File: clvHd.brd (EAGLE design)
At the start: 21 x 35 mm, 41 parts, among them IC1 LMV324M, X1 009176002, X2 009176002, X3 SSW-101-02-G-S, X4 009176002, X5 SSW-101-02-G-S, X6 009176002, X7 SSW-101-02-G-S

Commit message: update
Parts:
- removed A1, A2: 0R-JUMPC, jump-0r-smd:C0R-JMP
- removed ADC: MICROCHIP_MCP3427-E-UNMICROCHIP_MCP3427-E-UN_0_0, UN:MICROCHIP_MCP3427-E-UN_0
- removed C1, C3, C4, C5, C6, C7, C8, C9: 0.1nF, rcl:C0201
- removed C2: 1nF, rcl:C0201
- removed D3: HSMS-285C, avago:SOT323
- removed IC1: LMV324M, linear:SO14
- removed L: (no value), led:CHIP-LED0603
- removed P_AMP: INA326EA/250, INA326EA_250:SOP65P490X110-8N
- removed R1, R10, R11, R12, R13, R14, R16, R17, R2, R3, R4, R5, R6, R7, R8, R9: 100k, rcl:R0201
- removed R15: (no value), rcl:R0201
- removed TLE: TLE2426CD, tle2426:SO-8
- removed X1, X2, X4, X6: 009176002, con-avxPerso:009176002
- removed X3, X5, X7: SSW-101-02-G-S, con-samtec:SSW-101-02-G-S
- added LED1, LED2, LED3: (no value), led:CHIP-LED0603
- added PAD1, PAD10, PAD11, PAD12, PAD2, PAD3, PAD4, PAD5, PAD6, PAD7, PAD8, PAD9: WIREPADSMD1,27-254, wirepad:SMD1,27-2,54
- added U1: ADS1298CZXGR, ADS1298ZXGR:ZXG64
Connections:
- removed net GNDA: ADC.2, ADC.5, C2.1, IC1.12, IC1.3, IC1.5, R12.1, R2.1, R5.2, TLE.1, X7.1
- removed net INM: P_AMP.2, X3.1
- removed net INP: P_AMP.3, X5.1
- removed net N$1: P_AMP.1, R1.1
- removed net N$10: IC1.6, R6.2, R7.1, R8.1
- removed net N$11: D3.2, R14.2, R8.2
- removed net N$12: IC1.9, R10.1, R9.2
- removed net N$13: D3.3, IC1.7
- removed net N$14: D3.1, R7.2, R9.1
- removed net N$15: IC1.8, R10.2, R11.1
- removed net N$16: ADC.1, C5.2, IC1.14, R4.2
- removed net N$17: ADC.7, R16.2, X2.1, X6.1
- removed net N$18: IC1.10, R12.2, R14.1
- removed net N$2: P_AMP.8, R1.2
- removed net N$23: ADC.4, C4.1, IC1.1, R3.2, R6.1
- removed net N$4: C2.2, P_AMP.5, R2.2
- removed net N$54: L.A, R15.2
- removed net N$55: C7.1, TLE.8
- removed net N$56: ADC.8, R17.2, X2.2, X6.2
- removed net N$57: A1.2, ADC.9
- removed net N$58: A2.2, ADC.10
- removed net N$6: C3.1, IC1.2, R3.1
- removed net N$7: C3.2, C4.2, R13.2, R5.1
- removed net N$8: C5.1, IC1.13, R11.2, R4.1
- removed net N$9: P_AMP.6, R13.1
- removed net V+: A1.3, A2.3, ADC.6, C1.1, C6.1, C8.2, C9.2, IC1.4, P_AMP.7, R15.1, R16.1, R17.1, TLE.3, X1.2, X4.2
- removed net V-: A1.1, A2.1, ADC.3, C1.2, C6.2, C7.2, C8.1, C9.1, IC1.11, L.C, P_AMP.4, TLE.2, X1.1, X4.1
- new net IN1: U1.H1
- new net IN2: U1.G1
- new net REF: U1.G2, U1.H2
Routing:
- net V-: track 99.1 -> 0.00 mm, vias 7 -> 0
- net V+: track 84.2 -> 0.00 mm
- net N$17: track 44.6 -> 0.00 mm, vias 3 -> 0
- net GNDA: track 36.9 -> 0.00 mm, vias 5 -> 0
- net N$56: track 34.4 -> 0.00 mm, vias 3 -> 0
- net INP: track 34.3 -> 0.00 mm, vias 1 -> 0
- net N$9: track 25.4 -> 0.00 mm, vias 0 -> 1
- net N$23: track 23.5 -> 0.00 mm, vias 2 -> 0
- net N$8: track 17.8 -> 0.00 mm, vias 2 -> 1
- net N$10: track 16.8 -> 0.00 mm, vias 2 -> 1
- net N$6: track 13.3 -> 0.00 mm, vias 0 -> 1
- net N$12: track 12.1 -> 0.00 mm, vias 0 -> 1
- net N$13: track 10.4 -> 0.00 mm, vias 0 -> 1
- net N$16: track 8.56 -> 0.00 mm, vias 0 -> 1
- net N$7: track 8.02 -> 0.00 mm, vias 0 -> 1
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- added copper zone on layer 16, net IN1
- added copper zone on layer 16, net IN3
- added copper zone on layer 16, net IN4
- added copper zone on layer 16, net IN5
- added copper zone on layer 16, net IN6
- added copper zone on layer 16, net IN7
- added copper zone on layer 16, net IN8
- added copper zone on layer 16, net IN9
- added copper zone on layer 16, net REF
- removed copper zone on layer 16, net GNDA
- removed copper zone on layer 16, net INM
- removed copper zone on layer 16, net INP
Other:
- board size 21 x 35 mm -> 31 x 24 mm
- board text removed: "+"
- board text removed: "ClvHd"
- board text removed: "E+"
- board text removed: "E-"
- board text removed: "GND"
- board text removed: "SCL"
- board text removed: "SDA"
- board text removed: "V++"
- board text removed: "v7"

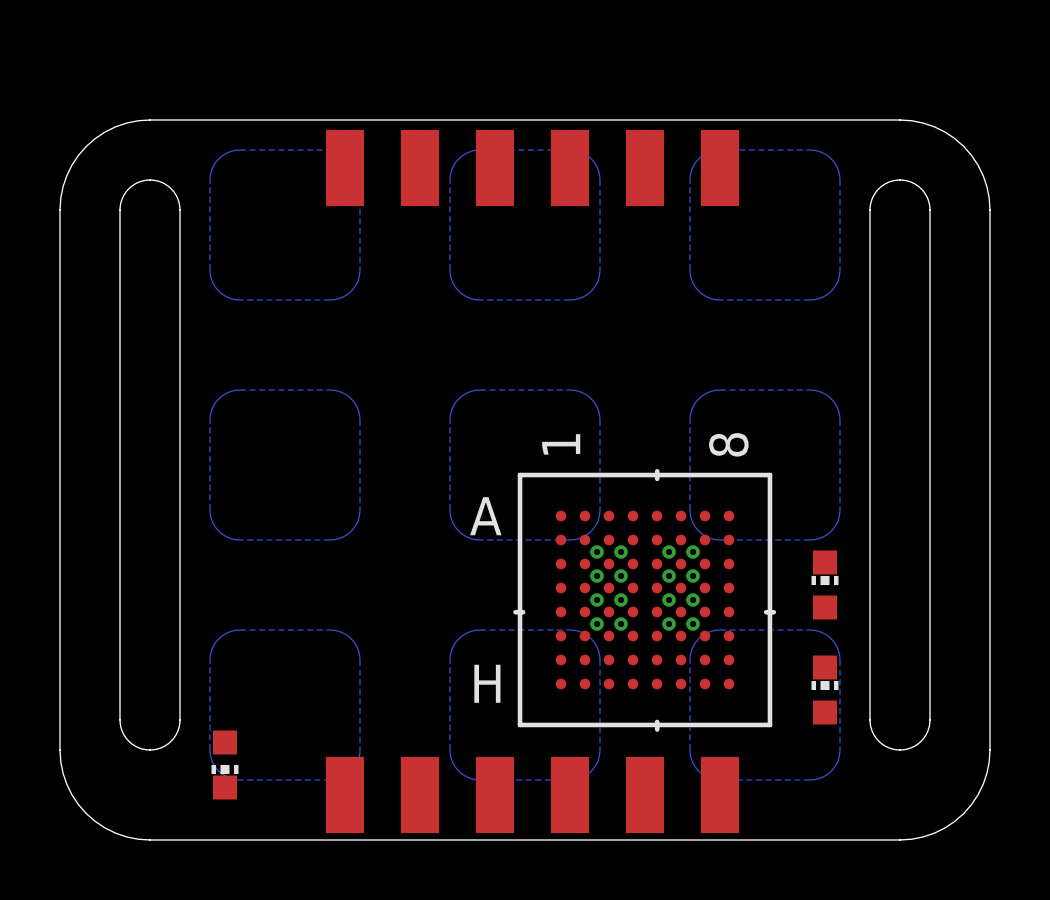
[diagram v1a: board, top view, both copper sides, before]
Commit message: jst sh conn
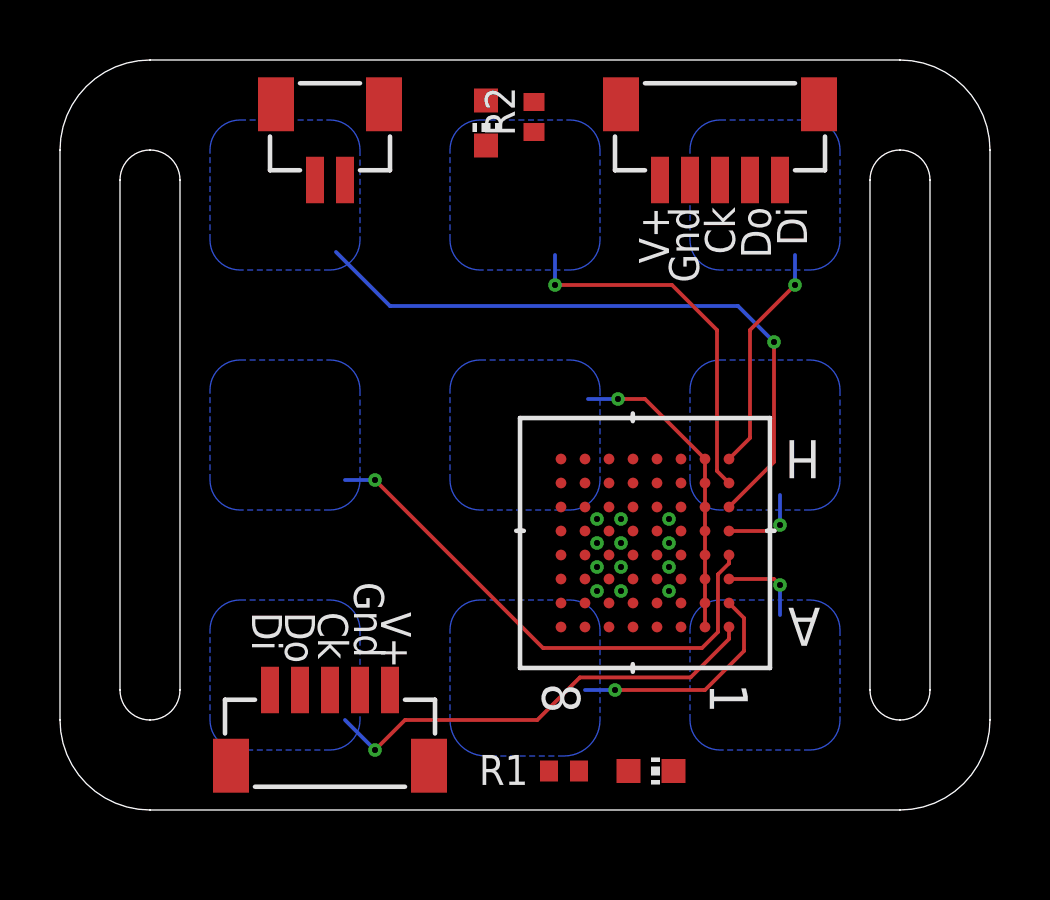
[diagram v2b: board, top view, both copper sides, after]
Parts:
- removed LED3: (no value), led:CHIP-LED0603
- removed PAD1, PAD10, PAD11, PAD12, PAD2, PAD3, PAD4, PAD5, PAD6, PAD7, PAD8, PAD9: WIREPADSMD1,27-254, wirepad:SMD1,27-2,54
- added R1, R2: (no value), rcl:R0402
- added X1: BM02B-SRSS-TB, con-JST SH:BM02B-SRSS-TB
- added X2, X3: BM05B-SRSS-TB, con-JST SH:BM05B-SRSS-TB
- moved LED2 22.0 mm to (14.2, 22.9), turned to 180 degrees
- moved LED1 14.2 mm to (19.7, 1.30), turned to 270 degrees
- moved U1 1.90 mm to (19.5, 8.90), turned to 180 degrees
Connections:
- new net CLK: X2.3, X3.3
- new net CS: U1.F7, X1.1
- new net DIN: X2.5, X3.5
- new net DOUT: X2.4, X3.4
- new net GND: R1.1, R2.1, X2.2, X3.2
- new net IN3: U1.C1
- new net IN4: U1.D1
- new net IN5: U1.E1
- new net IN6: U1.F1
- new net IN7: U1.G1
- new net IN8: U1.H1
- new net N$1: LED1.A, R1.2
- new net N$5: LED2.C, U1.F5
- new net N$6: LED2.A, R2.2
- new net V+: LED1.C, X2.1, X3.1
- net IN1: now also U1.A1; no longer U1.H1
- net IN2: now also U1.B1; no longer U1.G1
- net REF: now also U1.A2, U1.B2, U1.C2, U1.D2, U1.E2, U1.F2, X1.2
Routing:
- net IN6: track 0.00 -> 22.0 mm, vias 0 -> 1
- net IN4: track 0.00 -> 17.7 mm, vias 0 -> 1
- net IN1: track 0.00 -> 15.1 mm, vias 0 -> 1
- net IN7: track 0.00 -> 12.3 mm, vias 0 -> 1
- net REF: track 0.00 -> 10.3 mm, vias 0 -> 1
- net IN8: track 0.00 -> 7.71 mm, vias 0 -> 1
- net IN2: track 0.00 -> 7.65 mm, vias 0 -> 1
- net IN3: track 0.00 -> 2.78 mm, vias 0 -> 1
- net IN5: track 0.00 -> 2.78 mm, vias 0 -> 1
- added copper zone on layer 16, net IN2
- removed copper zone on layer 16, net IN9
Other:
- board size 31 x 24 mm -> 31 x 25 mm
- board text added: "Ck"
- board text added: "Di"
- board text added: "Do"
- board text added: "Gnd"
- board text added: "V+"

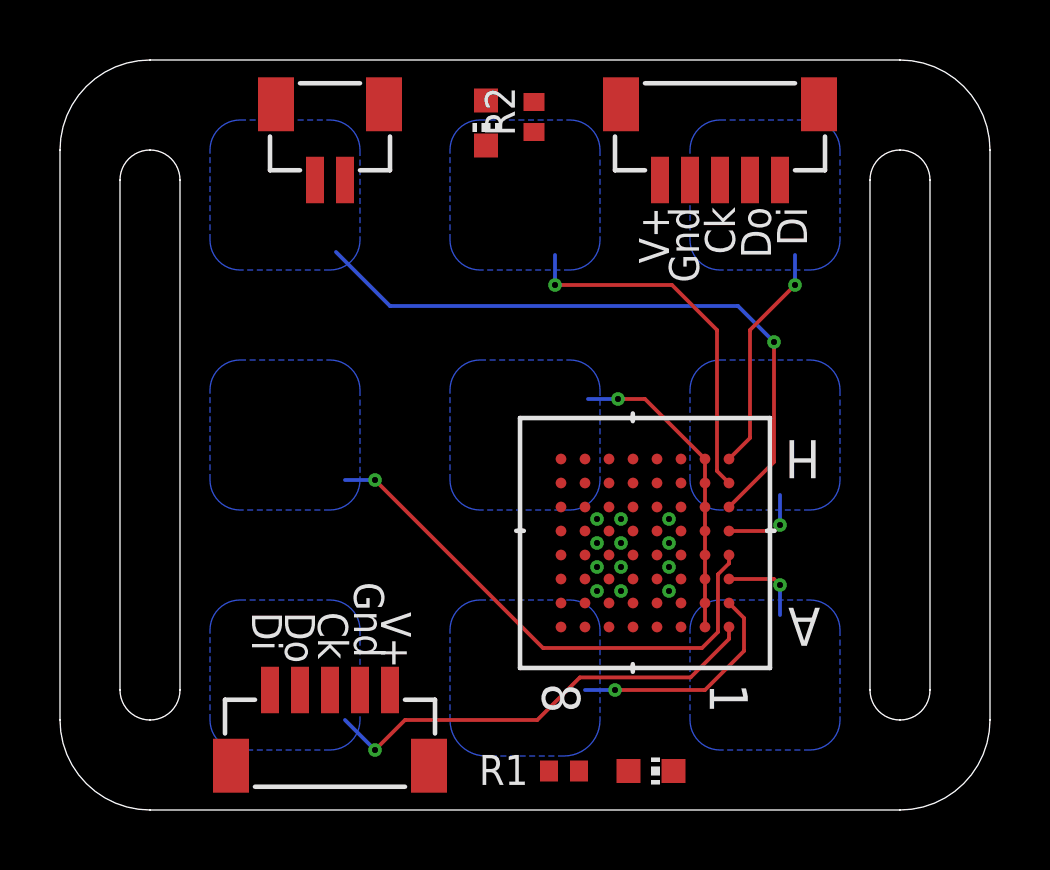
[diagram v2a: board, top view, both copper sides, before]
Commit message: dim changed to be panalized 3x4
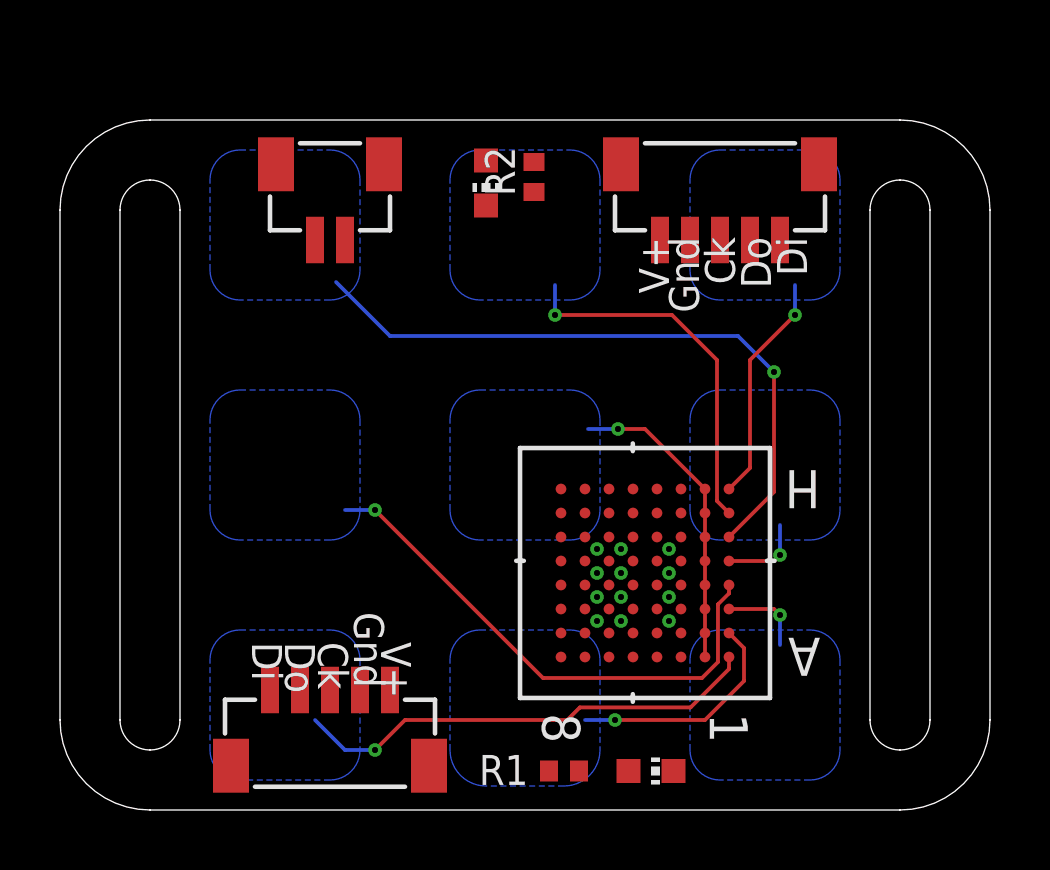
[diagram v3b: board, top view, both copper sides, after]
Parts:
- moved LED2 2.00 mm to (14.2, 20.9)
- moved R2 2.00 mm to (15.8, 21.1)
- moved X1 2.00 mm to (9.00, 19.0)
- moved X2 2.00 mm to (22.0, 19.0)
- moved U1 1.00 mm to (19.5, 7.90)
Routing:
- net IN1: track 15.1 -> 15.7 mm
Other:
- board size 31 x 25 mm -> 31 x 23 mm

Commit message: update
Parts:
- added C1, C10, C11, C12, C13, C14, C15, C16, C2, C3, C4, C5, C6, C7, C8, C9: 4.70nF, rcl:C0201
- added R10, R11, R12, R13, R14, R15, R16, R3, R4, R5, R6, R7, R8, R9: 4.99k, rcl:R0201
- R1, R2: value (none) -> 4.99k; device rcl:R0402 -> rcl:R0201
- U1: value ADS1298CZXGR -> ADS1299IPAG; device ADS1298ZXGR:ZXG64 -> ADS:PAG64_TEX
- X2, X3: value BM05B-SRSS-TB -> BM07B-SRSS-TB; device con-JST SH:BM05B-SRSS-TB -> con-JST SH:BM07B-SRSS-TB
- moved LED2 22.5 mm to (35.2, 12.9)
- moved R2 16.8 mm to (8.50, 6.00), turned to 0 degrees
- moved X2 16.3 mm to (9.50, 29.4)
- moved X1 13.4 mm to (17.5, 29.4)
- moved R1 12.2 mm to (5.50, 6.00)
- moved U1 9.01 mm to (16.8, 16.5), turned to 0 degrees
- moved LED1 4.24 mm to (15.7, 2.70), turned to 0 degrees
- moved X3 0.63 mm to (9.50, 3.61)
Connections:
- removed net CLK: X2.3, X3.3
- removed net IN1: U1.A1
- removed net IN2: U1.B1
- removed net IN3: U1.C1
- removed net IN4: U1.D1
- removed net IN5: U1.E1
- removed net IN6: U1.F1
- removed net IN7: U1.G1
- removed net IN8: U1.H1
- removed net REF: U1.A2, U1.B2, U1.C2, U1.D2, U1.E2, U1.F2, U1.G2, U1.H2, X1.2
- new net !PWDN: U1.35
- new net AVDD: U1.59
- new net AVDD1: U1.54
- new net AVDD_2: U1.19
- new net AVDD_3: U1.21
- new net AVDD_4: U1.22
- new net AVDD_5: U1.56
- new net AVSS: U1.58
- new net AVSS1: U1.53
- new net AVSS_2: U1.20
- new net AVSS_3: U1.23
- new net AVSS_4: U1.32
- new net AVSS_5: U1.57
- new net DGND: U1.51
- new net DGND_2: U1.33
- new net DGND_3: U1.49
- new net DVDD: U1.50
- new net DVDD_2: U1.48
- new net EL1N: R1.1
- new net EL1P: R2.1
- new net EL2N: R3.1
- new net EL2P: R4.1
- new net EL3N: R5.1
- new net EL3P: R6.1
- new net EL4N: R7.1
- new net EL4P: R8.1
- new net EL5N: R9.1
- new net EL5P: R10.1
- new net EL6N: R11.1
- new net EL6P: R12.1
- new net EL7N: R13.1
- new net EL7P: R14.1
- new net EL8N: R15.1
- new net EL8P: R16.1
- new net GNDA: C1.1, C10.1, C11.1, C12.1, C13.1, C14.1, C15.1, C16.1, C2.1, C3.1, C4.1, C5.1, C6.1, C7.1, C8.1, C9.1
- new net IN1N: C1.2, R1.2, U1.15
- new net IN1P: C2.2, R2.2, U1.16
- new net IN2N: C3.2, R3.2, U1.13
- new net IN2P: C4.2, R4.2, U1.14
- new net IN3N: C5.2, R5.2, U1.11
- new net IN3P: C6.2, R6.2, U1.12
- new net IN4N: C7.2, R7.2, U1.9
- new net IN4P: C8.2, R8.2, U1.10
- new net IN5N: C9.2, R9.2, U1.7
- new net IN5P: C10.2, R10.2, U1.8
- new net IN6N: C11.2, R11.2, U1.5
- new net IN6P: C12.2, R12.2, U1.6
- new net IN7N: C13.2, R13.2, U1.3
- new net IN7P: C14.2, R14.2, U1.4
- new net IN8N: C15.2, R15.2, U1.1
- new net IN8P: C16.2, R16.2, U1.2
- new net N$17: U1.36
- new net N$18: U1.37
- new net N$21: U1.47
- new net N$7: X1.2
- new net SCLK: U1.40, X2.3, X3.3
- net CS: now also U1.39; no longer U1.F7
- net DIN: now also U1.34
- net DOUT: now also U1.43
- net GND: no longer R1.1, R2.1
- net N$1: no longer R1.2
- net N$5: no longer U1.F5
- net N$6: no longer R2.2
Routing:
- net IN6: track 22.0 -> 0.00 mm, vias 1 -> 0
- net IN4: track 17.7 -> 0.00 mm, vias 1 -> 0
- net IN1: track 15.7 -> 0.00 mm, vias 1 -> 0
- net IN7: track 12.3 -> 0.00 mm, vias 1 -> 0
- net REF: track 10.3 -> 0.00 mm, vias 1 -> 0
- net IN8: track 7.71 -> 0.00 mm, vias 1 -> 0
- net IN2: track 7.65 -> 0.00 mm, vias 1 -> 0
- net IN3: track 2.78 -> 0.00 mm, vias 1 -> 0
- net IN5: track 2.78 -> 0.00 mm, vias 1 -> 0
- added copper zone on layer 16, net IN1P
- added copper zone on layer 16, net IN2P
- added copper zone on layer 16, net IN3P
- added copper zone on layer 16, net IN4P
- added copper zone on layer 16, net IN5P
- added copper zone on layer 16, net IN5P1
- added copper zone on layer 16, net IN6P
- added copper zone on layer 16, net IN7P
- added copper zone on layer 16, net IN7P1
- added copper zone on layer 16, net IN8P
- added copper zone on layer 16, net IN8P1
- removed copper zone on layer 16, net IN1
- removed copper zone on layer 16, net IN2
- removed copper zone on layer 16, net IN3
- removed copper zone on layer 16, net IN4
- removed copper zone on layer 16, net IN5
- removed copper zone on layer 16, net IN6
- removed copper zone on layer 16, net IN7
- removed copper zone on layer 16, net IN8
- removed copper zone on layer 16, net REF
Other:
- board size 31 x 23 mm -> 25 x 33 mm

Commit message: update
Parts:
- removed C14, C15: 4.70nF, rcl:C0201
- removed R16: 4.99k, rcl:R0201
- added C19, C20: 4.70nF, rcl:C0201
- added Q1: (no value), crystal:CTS406
- R10, R11, R12, R13, R14, R15, R9: value 4.99k -> 51
- U1: value ADS1299IPAG -> ADS1293CISQ/NOPB; device ADS:PAG64_TEX -> ADS:RSG28_3P6X3P6_TEX
- moved C16 109.7 mm to (-23.0, -84.0)
- moved LED2 100.6 mm to (-21.5, -70.2), turned to 0 degrees
- moved C13 100.2 mm to (-23.0, -58.5)
- moved C12 99.3 mm to (-23.0, -53.5)
- moved C11 92.9 mm to (-23.0, -63.5)
- moved R15 88.6 mm to (-23.0, -43.5)
- moved R14 88.0 mm to (-23.0, -38.5)
- moved R13 87.5 mm to (-23.0, -33.5)
- moved R12 86.9 mm to (-23.0, -28.5)
- moved R11 77.0 mm to (-23.0, -23.5)
- moved C10 76.9 mm to (-23.0, -18.5)
- moved C9 76.7 mm to (-23.0, -13.5)
- moved R10 68.0 mm to (-15.0, -8.50)
- moved R9 68.0 mm to (-15.0, -3.50)
- moved X2 17.9 mm to (3.61, 12.5), turned to 270 degrees
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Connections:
- removed net !PWDN: U1.35
- removed net AVDD: U1.59
- removed net AVDD1: U1.54
- removed net AVDD_2: U1.19
- removed net AVDD_3: U1.21
- removed net AVDD_4: U1.22
- removed net AVDD_5: U1.56
- removed net AVSS: U1.58
- removed net AVSS1: U1.53
- removed net AVSS_2: U1.20
- removed net AVSS_3: U1.23
- removed net AVSS_4: U1.32
- removed net AVSS_5: U1.57
- removed net DGND: U1.51
- removed net DGND_2: U1.33
- removed net DGND_3: U1.49
- removed net DVDD: U1.50
- removed net DVDD_2: U1.48
- removed net EL5N: R9.1
- removed net EL5P: R10.1
- removed net EL6N: R11.1
- removed net EL6P: R12.1
- removed net EL7N: R13.1
- removed net EL7P: R14.1
- removed net EL8N: R15.1
- removed net EL8P: R16.1
- removed net GND: X2.2, X3.2
- removed net IN5N: C9.2, R9.2, U1.7
- removed net IN5P: C10.2, R10.2, U1.8
- removed net IN6N: C11.2, R11.2, U1.5
- removed net IN6P: C12.2, R12.2, U1.6
- removed net IN7N: C13.2, R13.2, U1.3
- removed net IN7P: C14.2, R14.2, U1.4
- removed net IN8N: C15.2, R15.2, U1.1
- removed net IN8P: C16.2, R16.2, U1.2
- removed net N$17: U1.36
- removed net N$18: U1.37
- removed net N$21: U1.47
- removed net N$5: LED2.C
- removed net N$6: LED2.A
- new net ALARMB: LED2.A, U1.15
- new net CMOUT: R14.1, U1.8
- new net DRDYB: R13.1, R9.2
- new net GNDIO: C19.2, R11.2, U1.29, X2.2, X3.2
- new net N$10: R11.1, U1.21
- new net N$13: LED2.C, R12.1
- new net N$15: C11.1, R14.2, R15.2, U1.10
- new net N$2: R9.1, U1.20
- new net N$3: R10.1, U1.19
- new net N$4: C10.2, Q1.1, U1.23
- new net N$8: C9.2, Q1.3, U1.24
- new net N$9: C20.1, U1.26
- new net RLDIN: U1.11
- new net RLDOUT: C11.2, R15.1, U1.9
- new net RLDREF: C12.1, U1.12
- new net SYNCB: U1.13
- new net VCCIO: C19.1, R12.2, R13.2, U1.22
- new net VDD: C10.1, C13.1, C16.1, C9.1, U1.28
- new net VSSIO: U1.14
- new net WCT: U1.7
- net CS: now also U1.16; no longer U1.39
- net DIN: now also U1.18; no longer U1.34
- net DOUT: now also R10.2; no longer U1.43
- net GNDA: now also C12.2, C13.2, C16.2, C20.2, U1.27; no longer C10.1, C11.1, C12.1, C13.1, C14.1, C15.1, C16.1, C9.1
- net IN1N: now also U1.1; no longer U1.15
- net IN1P: now also U1.2; no longer U1.16
- net IN2N: now also U1.3; no longer U1.13
- net IN2P: now also U1.4; no longer U1.14
- net IN3N: now also U1.5; no longer U1.11
- net IN3P: now also U1.6; no longer U1.12
- net IN4N: no longer U1.9
- net IN4P: no longer U1.10
- net SCLK: now also U1.17; no longer U1.40
- net V+: no longer LED1.C
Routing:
- added copper zone on layer 16, net IN1P1
- added copper zone on layer 16, net IN1P2
- added copper zone on layer 16, net IN1P3
- removed copper zone on layer 16, net IN2P
- removed copper zone on layer 16, net IN3P
- removed copper zone on layer 16, net IN4P
- removed copper zone on layer 16, net IN5P
- removed copper zone on layer 16, net IN5P1
- removed copper zone on layer 16, net IN6P
- removed copper zone on layer 16, net IN7P
- removed copper zone on layer 16, net IN7P1
- removed copper zone on layer 16, net IN8P
- removed copper zone on layer 16, net IN8P1
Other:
- board size 25 x 33 mm -> 25 x 25 mm
